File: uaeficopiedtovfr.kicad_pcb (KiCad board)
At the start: 2 copper layers, 160 x 75 mm, 68 parts, among them J1 DTF13-12PB, J4 DTF13-12PB, J9 USB_C_Receptacle_USB2.0, M1 Module-power_12and5V-0.2, M2 Module-knock-0.2, M3 Module-vr-discrete-0.4, M4 Module-vr-max9924-0.1, M5 Module-wbo-0.5, M6 Module:mega-mcu100/0.2, M7 Module-wbo-0.5, P3 Pad, P4 Pad, Q1 ISL9V3040D3S, Q10 ZXMS6005SGTA, Q11 AO3400A, Q12 AO3400A, Q13 ZXMS6005SGTA, Q14 ZXMS6005SGTA, Q15 ZXMS6005SGTA, Q16 ZXMS6005SGTA, Q2 ISL9V3040D3S, Q3 ISL9V3040D3S, Q4 ISL9V3040D3S, Q7 ZXMS6005SGTA, Q8 ZXMS6005SGTA, Q9 ZXMS6005SGTA, U2 JDY-33

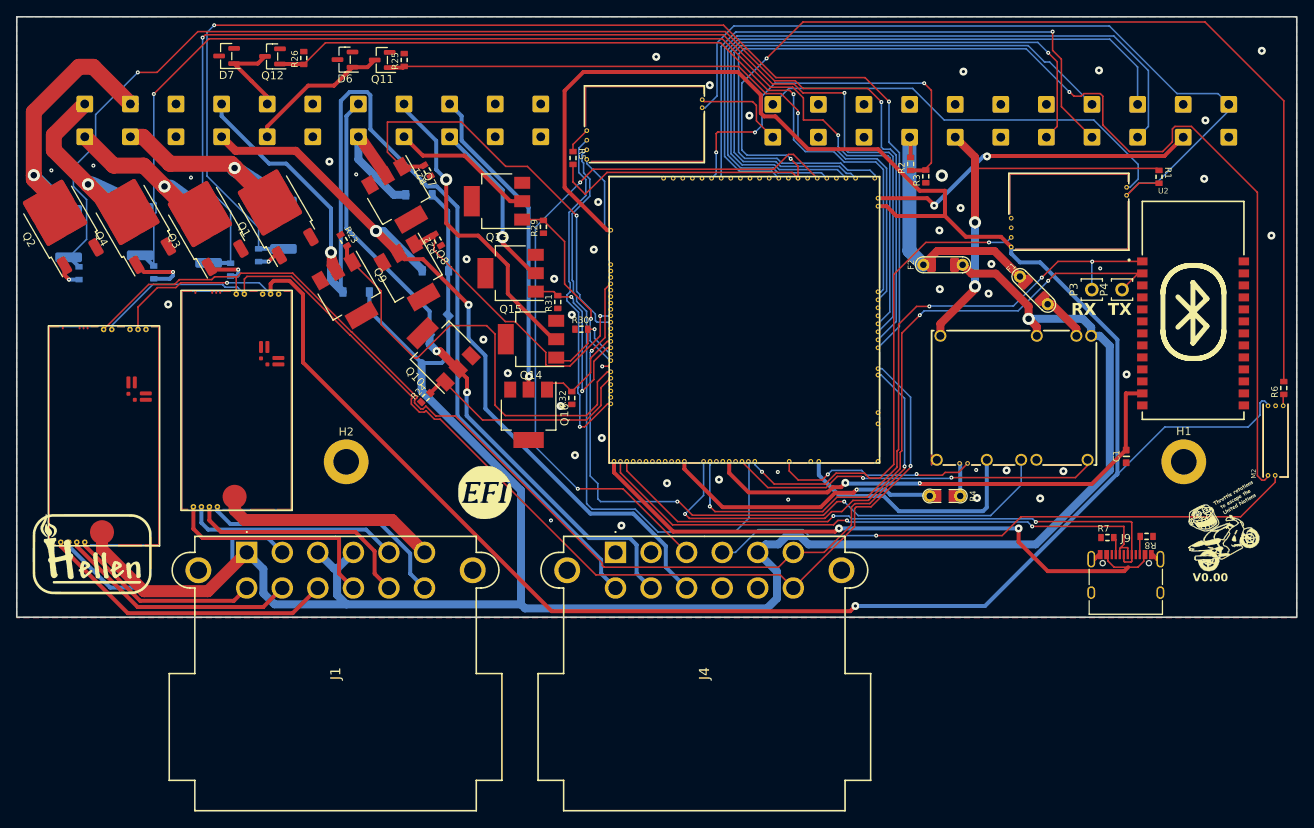
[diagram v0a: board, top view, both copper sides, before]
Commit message: Redesigned board to use 4 layers
module files are 4 layers, pointless to have the base board only be two
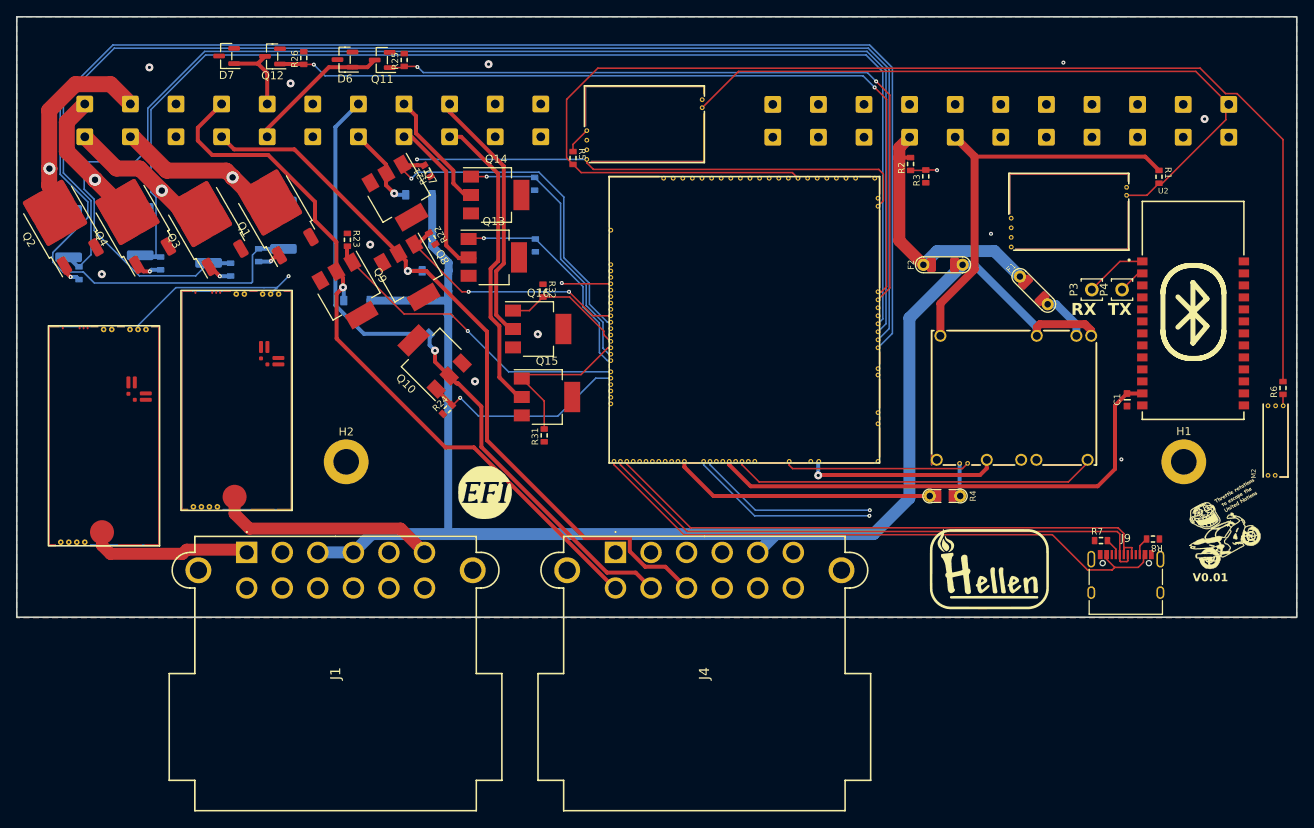
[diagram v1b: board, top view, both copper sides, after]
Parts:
- R29, R30: moved to B.Cu
- moved G4 112.2 mm to (123.7, 70.5)
- moved R30 19.1 mm to (66.5, 22.2), turned to 90 degrees
- moved Q14 18.5 mm to (61.8, 23.6), turned to 0 degrees
- moved R31 16.8 mm to (67.8, 53.7)
- moved Q15 16.1 mm to (68.1, 48.9), turned to 0 degrees
- moved R32 13.9 mm to (67.6, 35.6), turned to -90 degrees
- moved Q16 10.8 mm to (67.0, 40.4), turned to 0 degrees
- moved C1 7.08 mm to (140.6, 49.2)
- moved Q13 7.04 mm to (61.5, 31.4), turned to 0 degrees
- moved R24 3.08 mm to (55.6, 50.5)
- moved R29 2.53 mm to (66.7, 29.9)
- moved Q10 1.44 mm to (53.6, 44.0)
- moved R15 1.41 mm to (19.8, 32.2)
- moved D4 1.08 mm to (44.3, 36.9)
- moved R7 0.88 mm to (137.3, 66.8)
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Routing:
- net +5VA: track 325.5 -> 188.9 mm, vias 2 -> 3
- net /VREF1: track 146.8 -> 77.8 mm
- net +12V_RAW: track 252.3 -> 189.7 mm, vias 1 -> 0
- net /IAT_SENSOR: track 80.7 -> 28.3 mm, vias 1 -> 0
- net /IGN1: track 154.9 -> 201.1 mm, vias 2 -> 0
- net /OUT_LS3: track 138.1 -> 92.0 mm
- net /CLT: track 77.1 -> 34.1 mm
- net /IN_FLEX: track 92.3 -> 129.6 mm, vias 2 -> 0
- net /IN_TPS1: track 84.6 -> 49.6 mm
- net /INJOUT2: track 39.1 -> 15.7 mm, vias 1 -> 0
- net /INJ2: track 11.4 -> 34.2 mm
- net /IGN3: track 151.9 -> 171.8 mm, vias 2 -> 0
- net /IN_MAP: track 85.7 -> 66.0 mm
- net /IN_VMAIN: track 50.1 -> 32.8 mm, vias 3 -> 1
- net /LS3: track 57.5 -> 40.5 mm, vias 0 -> 1
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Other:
- copper layers 2 -> 4
- board text added: "V0.01"
- board text removed: "V0.00"
